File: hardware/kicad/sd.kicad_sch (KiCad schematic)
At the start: 1 part, among them J801 Micro_SD_Card

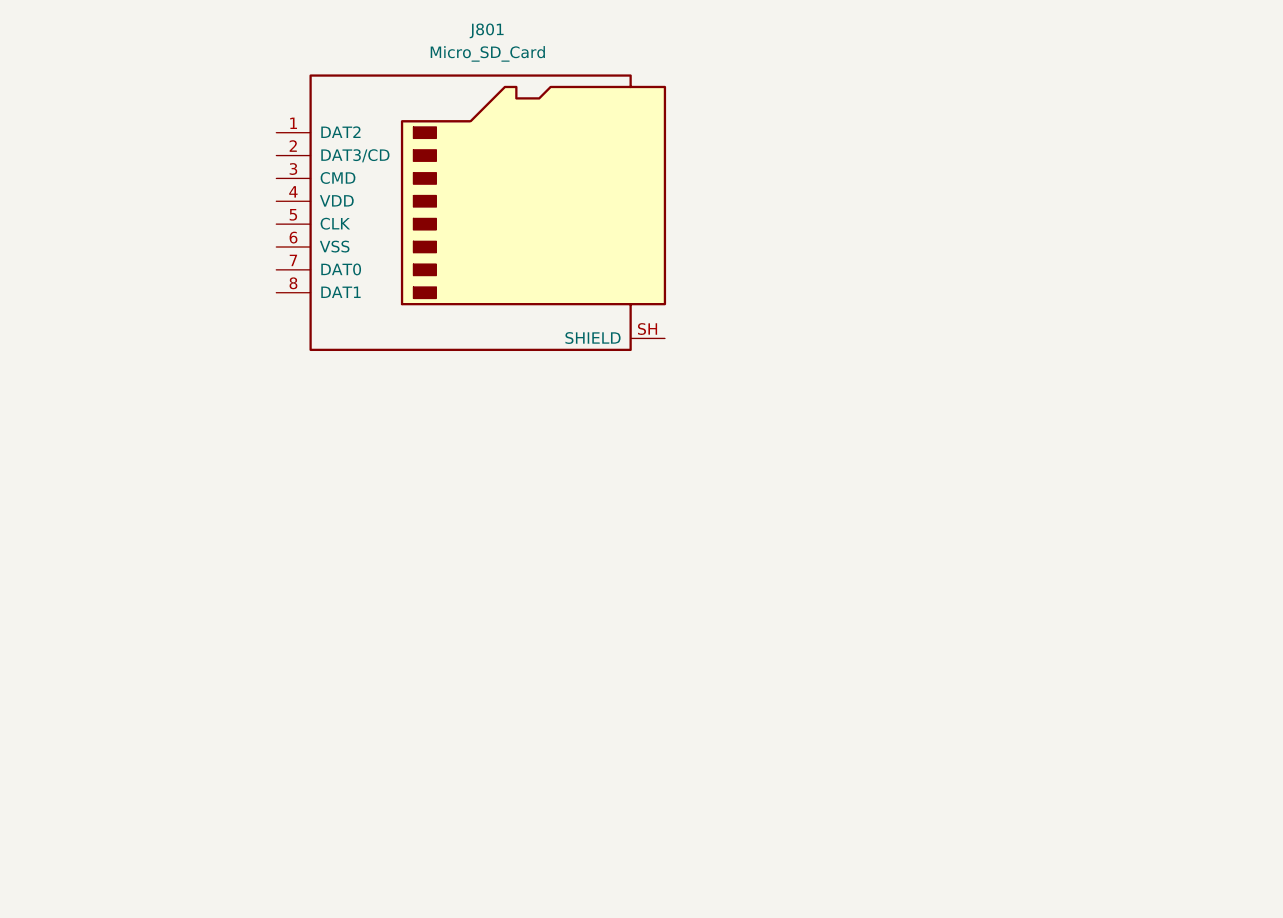
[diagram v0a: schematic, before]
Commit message: layout: finish dq0 & dq1 routing
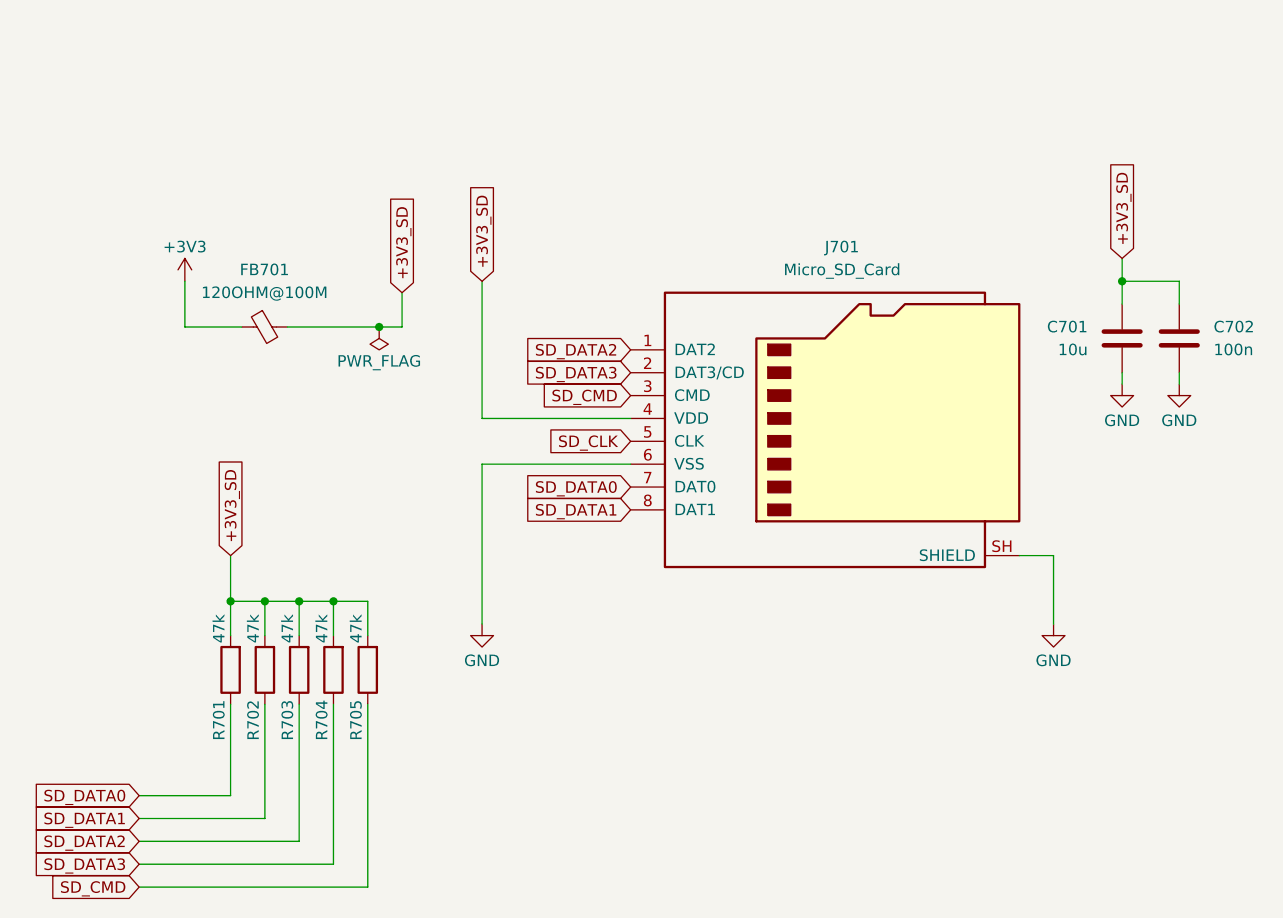
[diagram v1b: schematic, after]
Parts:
- added C701: 10u, Capacitor_SMD:C_0805_2012Metric, symbol Device:C
- added C702: 100n, Capacitor_SMD:C_0402_1005Metric, symbol Device:C
- added FB701: 120OHM@100M, Inductor_SMD:L_0402_1005Metric, symbol Device:FerriteBead_Small
- added R701, R702, R703, R704, R705: 47k, Resistor_SMD:R_0402_1005Metric, symbol Device:R
- renumbered J801 to J701
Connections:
- net SD_DATA2: now reaches J701.1 (DAT2)
- net SD_DATA2: now also R703.1
- net SD_DATA3: now reaches J701.2 (DAT3/CD)
- net SD_DATA3: now also R704.1
- net SD_CMD: now reaches J701.3 (CMD)
- net SD_CMD: now also R705.1
- net +3V3_SD: now reaches J701.4 (VDD)
- net +3V3_SD: now also C701.1, C702.1, FB701.2, R701.2, R702.2, R703.2, R704.2, R705.2
- net SD_CLK: now reaches J701.5 (CLK)
- net GND: now reaches J701.6 (VSS)
- net GND: now also J701.SH (SHIELD), C701.2, C702.2
- net SD_DATA0: now reaches J701.7 (DAT0)
- net SD_DATA0: now also R701.1
- net SD_DATA1: now reaches J701.8 (DAT1)
- net SD_DATA1: now also R702.1
- new net +3V3: FB701.1
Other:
- moved on the sheet: J701

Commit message: feat: need switch two singals of SD inferface
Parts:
- C701: footprint Capacitor_SMD:C_0805_2012Metric -> Capacitor_SMD:C_0603_1608Metric
- J701: footprint Projects:TF-SMD_503398-1892 -> Project:TF-SMD_TF-115-BCP9_LARG
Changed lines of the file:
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@@
 			)
 		)
-		(property "Footprint" "Projects:TF-SMD_503398-1892"
+		(property "Footprint" "Project:TF-SMD_TF-115-BCP9_LARG"
 			(at 203.2 81.28 0)
 			(hide yes)
@@
 			)
 		)
-		(property "Datasheet" "https://www.we-online.com/components/products/datasheet/693072010801.pdf"
+		(property "Datasheet" "C720505"
 			(at 173.99 88.9 0)
 			(hide yes)
@@
 			)
 		)
-		(property "Footprint" "Capacitor_SMD:C_0805_2012Metric"
+		(property "Footprint" "Capacitor_SMD:C_0603_1608Metric"
 			(at 204.7748 83.82 0)
 			(hide yes)
